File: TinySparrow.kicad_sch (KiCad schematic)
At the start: 13 parts, among them J1 LS_CONN, J2 RS_CONN, U1 STM32F103TBU6, U2 LD1117S33TR_SOT223, U3 SN65HVD230

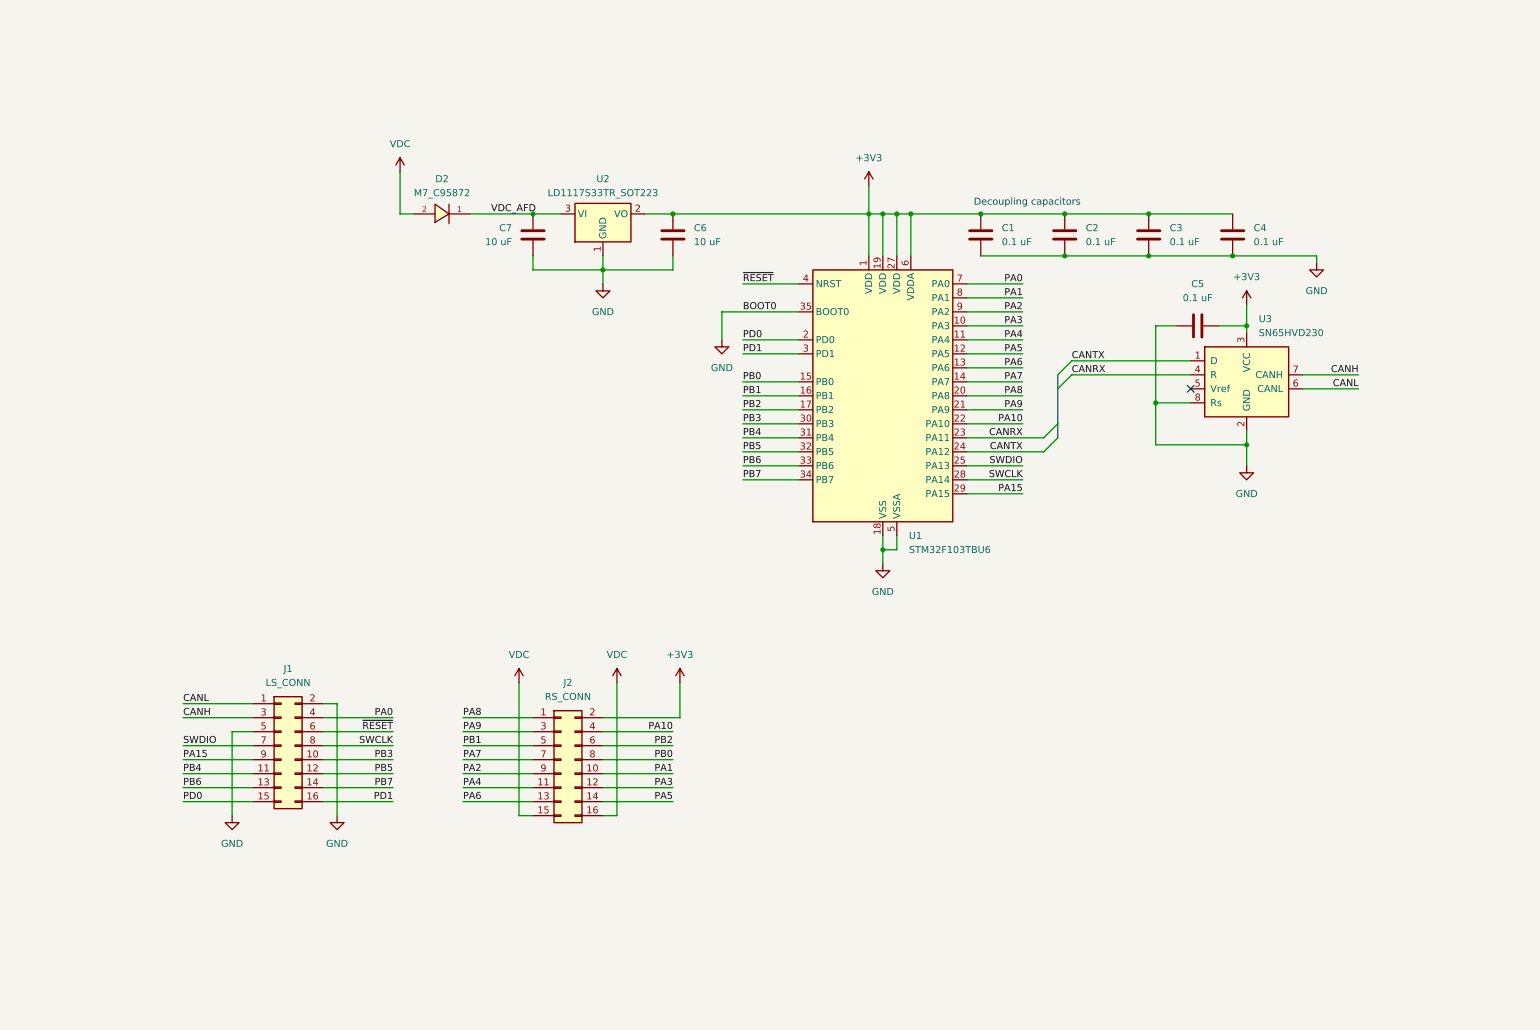
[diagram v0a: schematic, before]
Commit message: WIP: next generation TinySparrow with STM32G431 and CAN-FD
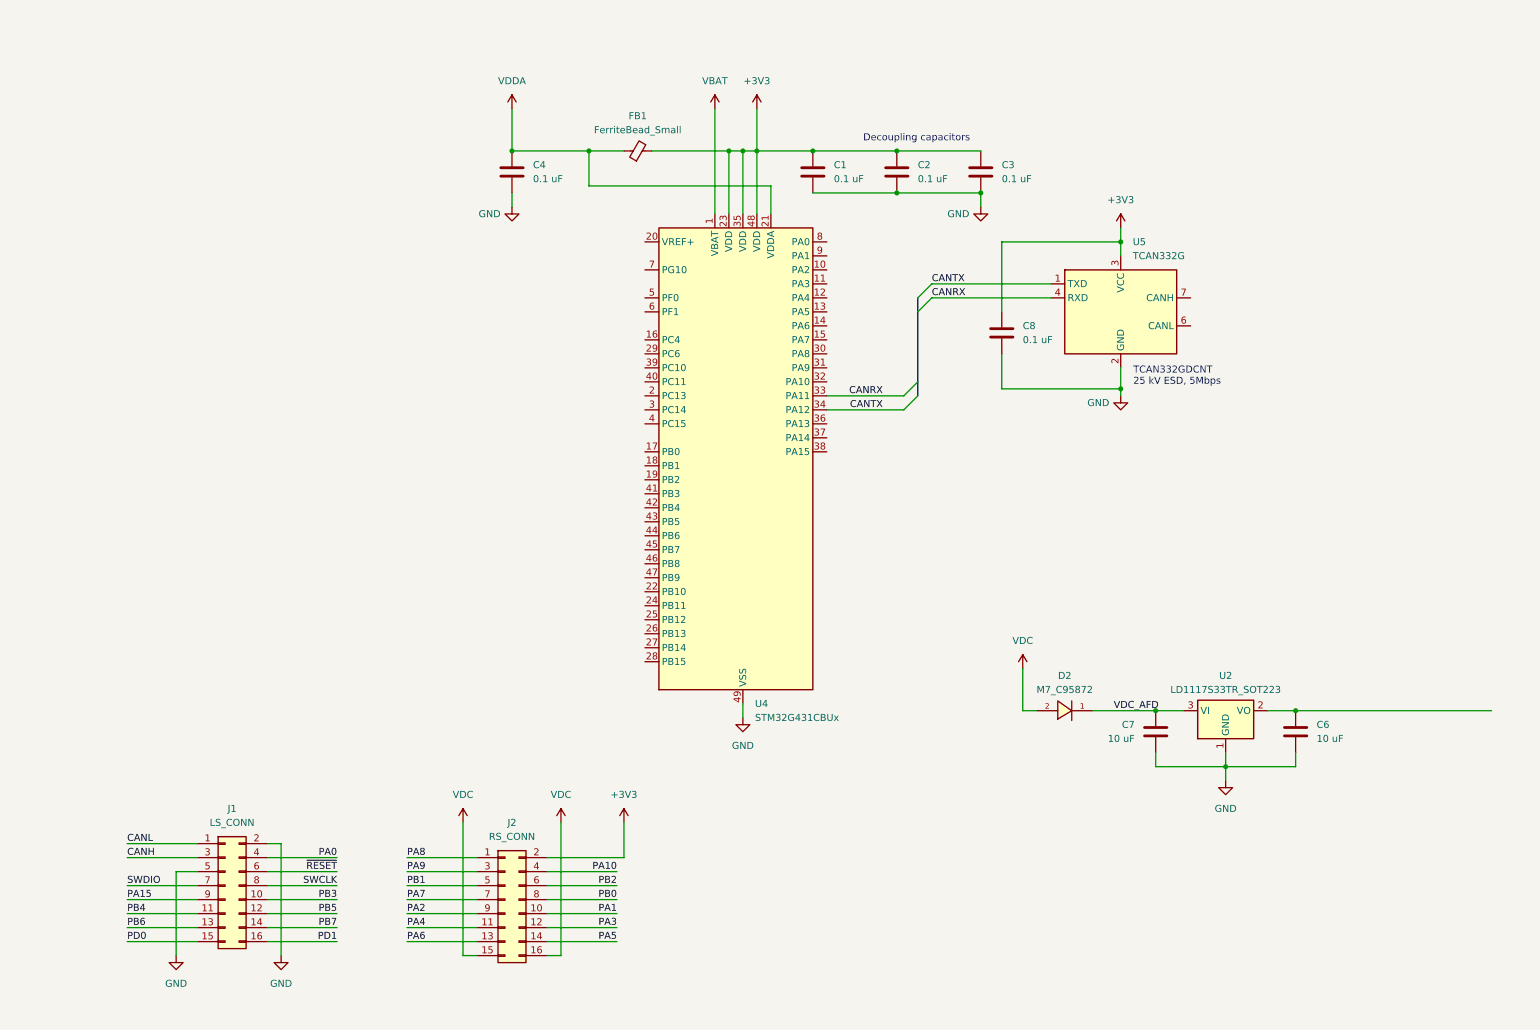
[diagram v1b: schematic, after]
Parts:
- removed C5: 0.1 uF, Capacitor_SMD:C_0603_1608Metric, symbol Device:C
- removed U1: STM32F103TBU6, Package_DFN_QFN:QFN-36-1EP_6x6mm_P0.5mm_EP4.1x4.1mm, symbol MCU_ST_STM32F1:STM32F103TBUx
- removed U3: SN65HVD230, Package_SO:SOIC-8_3.9x4.9mm_P1.27mm, symbol Interface_CAN_LIN:SN65HVD230
- added C8: 0.1 uF, Capacitor_SMD:C_0603_1608Metric, symbol Device:C
- added FB1: FerriteBead_Small, Inductor_SMD:L_0603_1608Metric, symbol Device:FerriteBead_Small
- added U4: STM32G431CBUx, Package_DFN_QFN:QFN-48-1EP_7x7mm_P0.5mm_EP5.6x5.6mm, symbol MCU_ST_STM32G4:STM32G431CBUx
- added U5: TCAN332G, Package_TO_SOT_SMD:TSOT-23-8, symbol Interface_CAN_LIN:TCAN332G
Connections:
- net +3V3: now also C8.1, FB1.2, U4.23 (VDD), U4.35 (VDD), U4.48 (VDD), U5.3 (VCC); no longer C4.2, C6.1, U2.2 (VO)
- net CANRX: now also U4.33 (PA11), U5.4 (RXD)
- net CANTX: now also U4.34 (PA12), U5.1 (TXD)
- net GND: now also C8.2, U4.49 (VSS), U5.2 (GND)
- new net: C6.1, U2.2 (VO)
- new net VBAT: U4.1 (VBAT)
- new net VDDA: C4.2, FB1.1, U4.21 (VDDA)
- no-connect marks 1 -> 0
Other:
- note added: "TCAN332GDCNT 25 kV ESD, 5Mbps"
- moved on the sheet: C1, C2, C3, C4, C6, C7, D2, J1, J2, U2

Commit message: NextGen: MCU upgrade to STM32G473CBT6
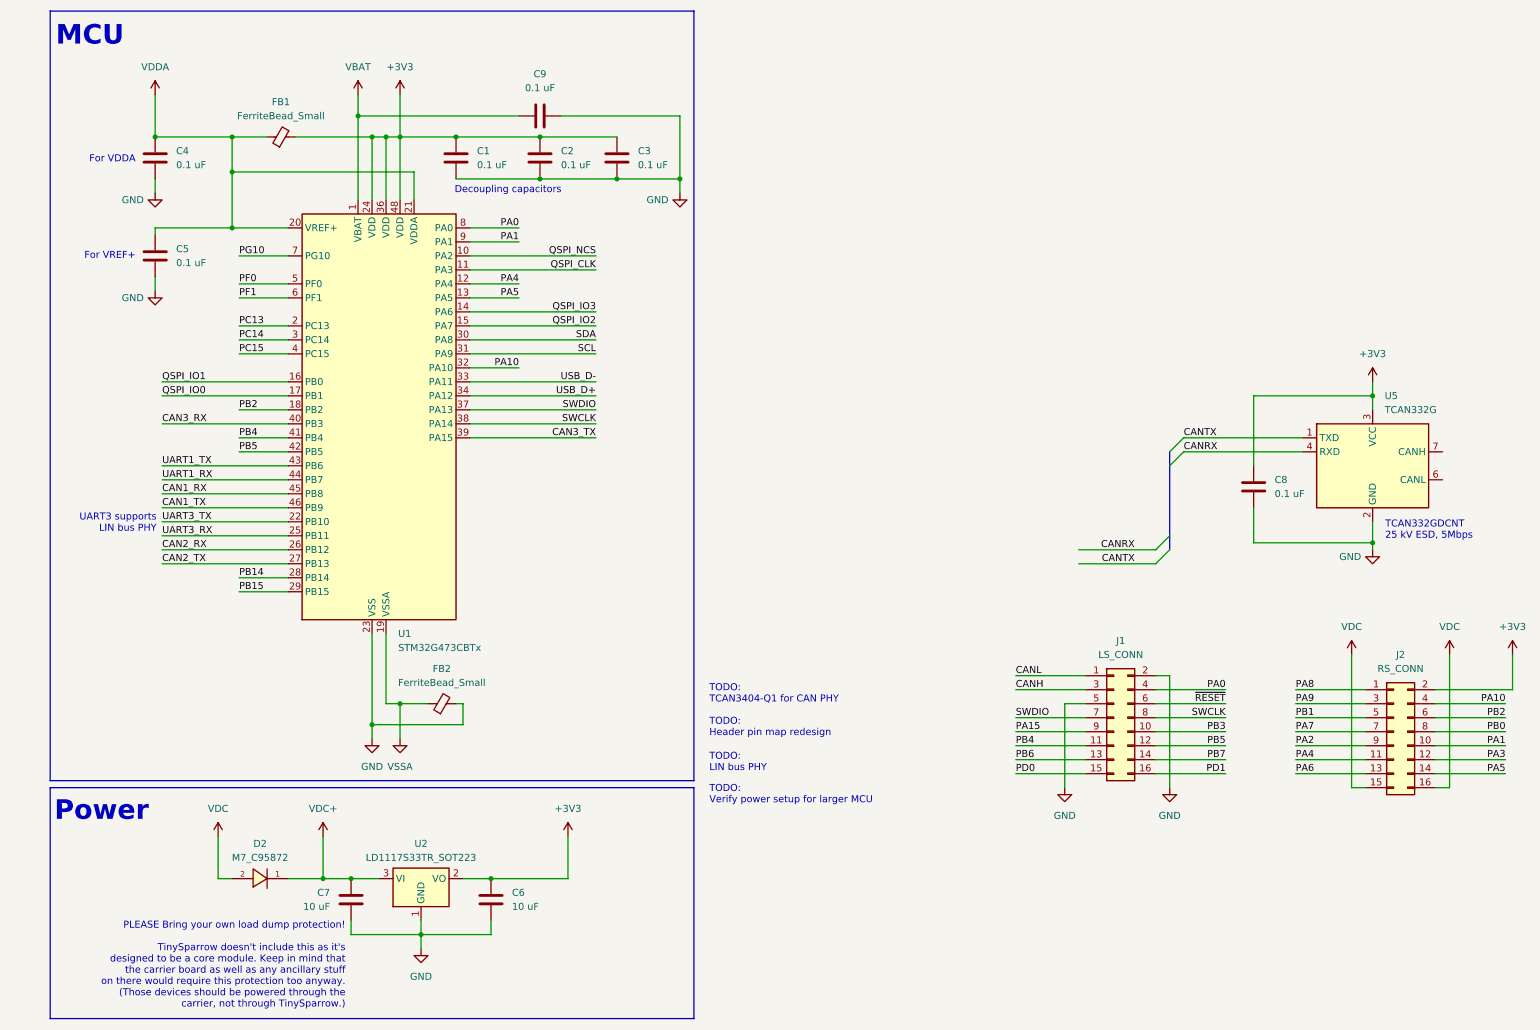
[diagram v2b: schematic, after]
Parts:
- removed U4: STM32G431CBUx, Package_DFN_QFN:QFN-48-1EP_7x7mm_P0.5mm_EP5.6x5.6mm, symbol MCU_ST_STM32G4:STM32G431CBUx
- added C5, C9: 0.1 uF, Capacitor_SMD:C_0603_1608Metric, symbol Device:C
- added FB2: FerriteBead_Small, Inductor_SMD:L_0603_1608Metric, symbol Device:FerriteBead_Small
- added U1: STM32G473CBTx, Package_QFP:LQFP-48_7x7mm_P0.5mm, symbol MCU_ST_STM32G4:STM32G473CBTx
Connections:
- net +3V3: now also C6.1, U2.2 (VO), U1.24 (VDD), U1.36 (VDD), U1.48 (VDD)
- net GND: now also C5.1, C9.1, FB2.2, U1.23 (VSS), U1.35 (VSS), U1.47 (VSS)
- net PA0: now also U1.8 (PA0)
- net PA1: now also U1.9 (PA1)
- net PA10: now also U1.32 (PA10)
- net PA4: now also U1.12 (PA4)
- net PA5: now also U1.13 (PA5)
- net PB2: now also U1.18 (PB2)
- net PB4: now also U1.41 (PB4)
- net PB5: now also U1.42 (PB5)
- net SWCLK: now also U1.38 (PA14)
- net SWDIO: now also U1.37 (PA13)
- net VBAT: now also C9.2, U1.1 (VBAT)
- net VDDA: now also C5.2, U1.20 (VREF+), U1.21 (VDDA)
- net VDC_AFD renamed VDC+
- new net CAN1_RX: U1.45 (PB8)
- new net CAN1_TX: U1.46 (PB9)
- new net CAN2_RX: U1.26 (PB12)
- new net CAN2_TX: U1.27 (PB13)
- new net CAN3_RX: U1.40 (PB3)
- new net CAN3_TX: U1.39 (PA15)
- new net PB14: U1.28 (PB14)
- new net PB15: U1.29 (PB15)
- new net PC13: U1.2 (PC13)
- new net PC14: U1.3 (PC14)
- new net PC15: U1.4 (PC15)
- new net PF0: U1.5 (PF0)
- new net PF1: U1.6 (PF1)
- new net PG10: U1.7 (PG10)
- new net QSPI_CLK: U1.11 (PA3)
- new net QSPI_IO0: U1.17 (PB1)
- new net QSPI_IO1: U1.16 (PB0)
- new net QSPI_IO2: U1.15 (PA7)
- new net QSPI_IO3: U1.14 (PA6)
- new net QSPI_NCS: U1.10 (PA2)
- new net SCL: U1.31 (PA9)
- new net SDA: U1.30 (PA8)
- new net UART1_RX: U1.44 (PB7)
- new net UART1_TX: U1.43 (PB6)
- new net UART3_RX: U1.25 (PB11)
- new net UART3_TX: U1.22 (PB10)
- new net USB_D+: U1.34 (PA12)
- new net USB_D-: U1.33 (PA11)
- new net VSSA: FB2.1, U1.19 (VSSA)
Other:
- note added: "For VDDA"
- note added: "For VREF+"
- note added: "MCU"
- note added: "PLEASE Bring your own load dump protection! TinySparrow doesn't include this as it's designed to be a core module. Keep in mind that the carrier board as well as any ancillary stuff on there would require this protection too anyway. (Those devices should be powered through the carrier, not through TinySparrow.)"
- note added: "Power"
- note added: "TODO: Header pin map redesign"
- note added: "TODO: LIN bus PHY"
- note added: "TODO: TCAN3404-Q1 for CAN PHY"
- note added: "TODO: Verify power setup for larger MCU"
- note added: "UART3 supports LIN bus PHY"
- title: TinySPARROW CAN MCU core board -> TinySPARROW-NG CAN MCU core board
- moved on the sheet: C1, C2, C3, C4, C6, C7, C8, D2, FB1, J1, J2, U2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
